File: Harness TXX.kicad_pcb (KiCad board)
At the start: 2 copper layers, 72.1 x 49.5 mm, 88 parts, among them J1 InpConn, J2 InSig, J3 OutConn, J6 SWD, SW1 SW_DPDT, SW2 SW_SPDT, U1 STM32F105RCTx, U2 SN65HVD230, U3 SN65HVD230, U4 TPS562200, U5 AMS1117-3.3, Y1 16MHz

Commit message: Workday progress
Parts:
- removed C18: 10p, Capacitor_SMD:C_0603_1608Metric
- removed C20: 10uF, Capacitor_SMD:C_0603_1608Metric_Pad1.08x0.95mm_HandSolder
- removed C23, C24, C26: 22uF, Capacitor_SMD:C_0603_1608Metric_Pad1.08x0.95mm_HandSolder
- removed C25: 1uF, Capacitor_SMD:C_0603_1608Metric_Pad1.08x0.95mm_HandSolder
- removed JP3, JP4: , Jumper:SolderJumper-2_P1.3mm_Bridged2Bar_Pad1.0x1.5mm
- removed PWR_3V1, PWR_IN1, PWR_IN2: LED, LED_SMD:LED_0603_1608Metric_Pad1.05x0.95mm_HandSolder
- removed PWR_5V1: 100, Resistor_SMD:R_0603_1608Metric_Pad0.98x0.95mm_HandSolder
- removed R14, R16, R20: 120, Resistor_SMD:R_0603_1608Metric
- removed R18: 47, Resistor_SMD:R_0603_1608Metric
- removed R24: 10K, Resistor_SMD:R_0603_1608Metric_Pad0.98x0.95mm_HandSolder
- removed R25: 54.9K, Resistor_SMD:R_0603_1608Metric_Pad0.98x0.95mm_HandSolder
- removed R5, R6, R7: 2k2, Resistor_SMD:R_0603_1608Metric
- removed R8: 100, Resistor_SMD:R_0603_1608Metric
- removed TP2, TP4, TP6, TP8: , TestPoint:TestPoint_THTPad_1.0x1.0mm_Drill0.5mm
- removed U5: AMS1117-3.3, Package_TO_SOT_SMD:SOT-223-3_TabPin2
- added D10: SMLVN6RGB, LED_SMD:LED_ROHM_SMLVN6, F.Cu at (81.5, 80.5)
- added D7: LED, LED_SMD:LED_0603_1608Metric_Pad1.05x0.95mm_HandSolder, F.Cu at (87.4, 71.5)
- added D8: RED, LED_SMD:LED_0603_1608Metric, F.Cu at (97.8, 73.4)
- added D9: DT1446-04TS-7, Global Libraries:SOT95P280X100-6N, F.Cu at (104.4, 80.8)
- added J4: Conn_01x02, Connector_PinHeader_2.54mm:PinHeader_1x02_P2.54mm_Vertical, F.Cu at (111.5, 87.6)
- added SW3: SW_SPDT, Connector_PinHeader_1.27mm:PinHeader_1x03_P1.27mm_Vertical, F.Cu at (98.6, 80.0)
- C1: value 4u7 -> 10uF; footprint Capacitor_SMD:C_0603_1608Metric -> Capacitor_SMD:C_0603_1608Metric_Pad1.08x0.95mm_HandSolder
- C10: value 0u1 -> 100n
- C11, C12, C13, C14: value 100p -> 100n
- C15: value 4.7n -> 1u
- C16: value 4.7n -> 10n
- C17: value 10p -> 0u1
- C19: value 10uF -> 4.7n; footprint Capacitor_SMD:C_0603_1608Metric_Pad1.08x0.95mm_HandSolder -> Capacitor_SMD:C_0603_1608Metric
- C2: value 100n -> 10uF; footprint Capacitor_SMD:C_0603_1608Metric -> Capacitor_SMD:C_0603_1608Metric_Pad1.08x0.95mm_HandSolder
- C21, C22: value 100nF -> 10p; footprint Capacitor_SMD:C_0603_1608Metric_Pad1.08x0.95mm_HandSolder -> Capacitor_SMD:C_0603_1608Metric
- C3, C4: value 100n -> 100nF; footprint Capacitor_SMD:C_0603_1608Metric -> Capacitor_SMD:C_0603_1608Metric_Pad1.08x0.95mm_HandSolder
- C5, C6: value 100n -> 22uF; footprint Capacitor_SMD:C_0603_1608Metric -> Capacitor_SMD:C_0603_1608Metric_Pad1.08x0.95mm_HandSolder
- C7: value 1u -> 1uF; footprint Capacitor_SMD:C_0603_1608Metric -> Capacitor_SMD:C_0603_1608Metric_Pad1.08x0.95mm_HandSolder
- C8: value 10n -> 22uF; footprint Capacitor_SMD:C_0603_1608Metric -> Capacitor_SMD:C_0603_1608Metric_Pad1.08x0.95mm_HandSolder
- C9: value 0u1 -> 4u7
- D1: value 20V -> SD0603S040S0R2; footprint Diode_SMD:D_0603_1608Metric_Pad1.05x0.95mm_HandSolder -> SamacSys_Parts:SD0603
- D2: value 0.7dV -> SD0603S040S0R2; footprint Diode_SMD:D_0603_1608Metric_Pad1.05x0.95mm_HandSolder -> SamacSys_Parts:SD0603
- D3: value RED -> SD0603S040S0R2; footprint LED_SMD:LED_0603_1608Metric -> SamacSys_Parts:SD0603
- D4: value SMLVN6RGB -> SD0603S040S0R2; footprint LED_SMD:LED_ROHM_SMLVN6 -> SamacSys_Parts:SD0603
- D5: value CD143A-SR05 -> 32V; footprint SamacSys_Parts:CD143ASR05 -> Diode_SMD:D_SOD-323
- D6: value CD143A-SR05 -> 0.7dV; footprint SamacSys_Parts:CD143ASR05 -> Diode_SMD:D_SMA
- F1: footprint Fuse:Fuse_0603_1608Metric_Pad1.05x0.95mm_HandSolder -> Fuse:Fuse_1206_3216Metric_Pad1.42x1.75mm_HandSolder
- J1: value InpConn -> DEUTSCH DT Inp; footprint SamacSys_Parts:348300801 -> Global Libraries:DT13-6P
- J2: value InSig -> DEUTSCH DT Data; footprint SamacSys_Parts:348300801 -> Global Libraries:DT13-6P
- J3: value OutConn -> DEUTSCH DT Out; footprint SamacSys_Parts:348300801 -> Global Libraries:DT13-6P
- L1: value 68n -> 4u7; footprint Inductor_SMD:L_0603_1608Metric -> Inductor_SMD:L_Sunlord_MWSA0518_5.4x5.2mm
- L2: value 4u7 -> 68n; footprint Inductor_SMD:L_Sunlord_MWSA0518_5.4x5.2mm -> Inductor_SMD:L_0603_1608Metric
- R1: value Rterm -> 10K; moved to F.Cu
- R12: value 120 -> 220
- R2: value 470 -> 10K
- R21: value 10K -> 47
- R22: value 22 -> 10K
- R23: value 10K -> 22; footprint Resistor_SMD:R_0603_1608Metric_Pad0.98x0.95mm_HandSolder -> Resistor_SMD:R_0603_1608Metric
- R3: value 0 -> 54.9K
- R4: value 2k2 -> 470R; footprint Resistor_SMD:R_0603_1608Metric -> Resistor_SMD:R_0603_1608Metric_Pad0.98x0.95mm_HandSolder
- R9: value 220 -> 100
- SW1: value SW_DPDT -> CAS-120B; footprint SamacSys_Parts:JS202011JCQN -> SamacSys_Parts:CAS120B
- SW2: value SW_SPDT -> CAS-120B; footprint Connector_PinHeader_1.27mm:PinHeader_1x03_P1.27mm_Vertical -> SamacSys_Parts:CAS120B
- U1: value STM32F105RCTx -> LMR51420; footprint Package_QFP:LQFP-64_10x10mm_P0.5mm -> Package_TO_SOT_SMD:SOT-23-6
- U2: value SN65HVD230 -> AMS1117-3.3; footprint Package_SO:SOIC-8_3.9x4.9mm_P1.27mm -> Package_TO_SOT_SMD:SOT-223-3_TabPin2
- U3: value SN65HVD230 -> STM32F105RCTx; footprint Package_SO:SOIC-8_3.9x4.9mm_P1.27mm -> Package_QFP:LQFP-64_10x10mm_P0.5mm
- U4: value TPS562200 -> SN65HVD230; footprint Package_TO_SOT_SMD:SOT-23-6 -> Package_SO:SOIC-8_3.9x4.9mm_P1.27mm
- moved SW1 93.9 mm to (76.7, 94.7), turned to 0 degrees
- moved U2 75.4 mm to (104.9, 74.9), turned to 180 degrees
- moved SW2 75.1 mm to (111.0, 95.5)
- moved C5 73.8 mm to (109.4, 69.3)
- moved D4 68.8 mm to (97.8, 96.5), turned to 180 degrees
- moved D3 66.6 mm to (100.8, 96.5), turned to 180 degrees
- moved J3 65.2 mm to (115.0, 86.6), turned to 180 degrees
- moved U1 63.4 mm to (95.2, 70.0), turned to -90 degrees
- moved JP1 62.2 mm to (104.9, 84.7), turned to 90 degrees
- moved R19 62.1 mm to (107.9, 85.4)
- moved R3 62.0 mm to (98.8, 70.9), turned to 0 degrees
- moved F1 59.1 mm to (74.7, 72.6), turned to -90 degrees
- moved J6 58.3 mm to (98.7, 93.0), turned to 180 degrees
- moved C17 57.4 mm to (102.0, 90.0)
- moved C6 57.4 mm to (109.4, 67.6)
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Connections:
- C1 pad 1: +3.3V -> /VRM/BUCK/V_in
- C11 pad 1: Net-(C11-Pad1) -> +3V3
- C12 pad 1: Net-(C12-Pad1) -> +3V3
- C13 pad 1: Net-(C13-Pad1) -> +3V3
- C14 pad 1: Net-(C14-Pad1) -> +3V3
- C15 pad 1: GND -> +3.3VA
- C15 pad 2: Net-(C15-Pad2) -> GND
- C16 pad 1: GND -> +3.3VA
- C16 pad 2: Net-(C16-Pad2) -> GND
- C17 pad 1: /MCU/HSE_in -> +3V3
- C19 pad 1: /VRM/12V_Out_Protected -> GND
- C19 pad 2: GND -> Net-(C19-Pad2)
- C2 pad 1: +3.3V -> /VRM/BUCK/V_in
- C21 pad 1: /VRM/12V_Out_Protected -> /MCU/HSE_in
- C22 pad 1: /VRM/BUCK/SW -> Net-(C22-Pad1)
- C22 pad 2: /VRM/BUCK/VBST -> GND
- C3 pad 1: +3.3V -> /VRM/BUCK/V_in
- C4 pad 1: +3.3V -> /VRM/BUCK/SW
- C4 pad 2: GND -> /VRM/BUCK/VBST
- C5 pad 1: +3.3V -> +5V
- C6 pad 1: +3.3V -> +5V
- C7 pad 1: +3.3VA -> +5V
- C8 pad 1: +3.3VA -> +3V3
- D1 pad 1: Net-(D1-Pad1) -> +3V3
- D1 pad 2: GND -> /WheelIn2
- D2 pad 1: /VRM/12V_Out_Protected -> /WheelIn2
- D2 pad 2: Net-(D1-Pad1) -> GND
- D3 pad 1: Net-(D3-Pad1) -> +3V3
- D3 pad 2: +3.3V -> /WheelIn1
- D4 pad 1: +3.3V -> /WheelIn1
- D4 pad 2: +3.3V -> GND
- D5 pad 1: GND -> /VRM/DIODE
- D5 pad 2: Net-(C11-Pad1) -> GND
- D6 pad 1: GND -> /VRM/BUCK/V_in
- D6 pad 2: Net-(C12-Pad1) -> /VRM/DIODE
- F1 pad 1: Net-(D1-Pad1) -> /VRM/DIODE
- F1 pad 2: +12V -> +24V
- J1 pad 1: /CAN- -> GND
- J1 pad 2: GND -> /CAN-
- J1 pad 3: +12V -> /PassThru1
- J1 pad 4: /WheelIn1 -> +24V
- J1 pad 6: GND -> /SHIELD
- J1 pad 7: /MISC -> (no net)
- J1 pad 8: /WheelIn2 -> (no net)
- J2 pad 1: +12V -> GND
- J2 pad 2: GND -> /WheelIn2
- J2 pad 3: /WheelIn2 -> /WheelIn1
- J2 pad 4: unconnected-(J2-Pad4) -> +24V
- J2 pad 5: unconnected-(J2-Pad5) -> +5V
- J2 pad 6: unconnected-(J2-Pad6) -> /Extra1
- J2 pad 7: unconnected-(J2-Pad7) -> (no net)
- J2 pad 8: unconnected-(J2-Pad8) -> (no net)
- J3 pad 1: /CAN+ -> GND
- J3 pad 2: GND -> /CAN-
- J3 pad 3: +12V -> /PassThru2
- J3 pad 4: /ENCD1 -> +24V
- J3 pad 5: /CAN- -> /CAN+
- J3 pad 6: GND -> /SHIELD
- J3 pad 7: /MISC -> (no net)
- J3 pad 8: /ENCD2 -> (no net)
- J6 pad 1: +3.3V -> +3V3
- JP1 pad 1: Net-(C13-Pad1) -> Net-(D9-Pad6)
- JP1 pad 2: /MCU/CAN1_H -> /CAN+
- JP2 pad 1: Net-(C11-Pad1) -> Net-(D9-Pad4)
- JP2 pad 2: /MCU/CAN1_L -> /CAN-
- L1 pad 1: +3.3V -> /VRM/BUCK/SW
- L1 pad 2: +3.3VA -> +5V
- L2 pad 1: /VRM/BUCK/SW -> +3V3
- L2 pad 2: /5V -> +3.3VA
- R1 pad 1: /CAN- -> /VRM/BUCK/V_in
- R1 pad 2: /CAN+ -> /VRM/BUCK/EN
- R10 pad 1: Net-(D4-Pad5) -> Net-(D10-Pad6)
- R10 pad 2: /MCU/LED_G -> /MCU/LED_B
- R11 pad 1: Net-(D4-Pad4) -> Net-(D10-Pad5)
- R11 pad 2: /MCU/LED_R -> /MCU/LED_G
- R12 pad 1: Net-(C15-Pad2) -> Net-(D10-Pad4)
- R12 pad 2: Net-(C11-Pad1) -> /MCU/LED_R
- R13 pad 1: Net-(C16-Pad2) -> Net-(C19-Pad2)
- R13 pad 2: Net-(C12-Pad1) -> Net-(D9-Pad4)
- R15 pad 1: Net-(C16-Pad2) -> Net-(C19-Pad2)
- R15 pad 2: Net-(C12-Pad1) -> Net-(D9-Pad4)
- R17 pad 1: Net-(C14-Pad1) -> Net-(D9-Pad6)
- R17 pad 2: Net-(J5-Pad2) -> Net-(J4-Pad2)
- R19 pad 1: Net-(C13-Pad1) -> Net-(D9-Pad6)
- R2 pad 1: /VRM/12V_Out_Protected -> /VRM/BUCK/VFB
- R2 pad 2: Net-(PWR_IN1-Pad2) -> GND
- R21 pad 1: Net-(R21-Pad1) -> /MCU/HSE_out
- R21 pad 2: /MCU/BOOT0 -> Net-(C22-Pad1)
- R22 pad 1: Net-(J6-Pad2) -> Net-(R22-Pad1)
- R22 pad 2: /MCU/SWDIO -> /MCU/BOOT0
- R23 pad 1: /VRM/12V_Out_Protected -> Net-(J6-Pad2)
- R23 pad 2: /VRM/BUCK/EN -> /MCU/SWDIO
- R3 pad 1: /3V3 -> /VRM/BUCK/VFB
- R3 pad 2: Net-(PWR_3V1-Pad2) -> +5V
- R4 pad 1: +3.3V -> GND
- R4 pad 2: /MCU/I2C1_SCL -> Net-(D7-Pad1)
- R9 pad 1: Net-(D4-Pad6) -> Net-(D8-Pad1)
- R9 pad 2: /MCU/LED_B -> GND
- SW1 pad 1: /ENCD1 -> /WheelIn1
- SW1 pad 2: /WheelIn2 -> /PassThru1
- SW1 pad 3: /ENCD2 -> /WheelIn2
- SW2 pad 1: +3.3V -> /WheelIn1
- SW2 pad 2: Net-(R21-Pad1) -> /PassThru2
- SW2 pad 3: GND -> /WheelIn2
- TP5 pad 1: Net-(C13-Pad1) -> Net-(D9-Pad6)
- TP7 pad 1: Net-(C11-Pad1) -> Net-(D9-Pad4)
- U1 pad 1: +3.3V -> GND
- U1 pad 2: /MCU/PC13 -> /VRM/BUCK/SW
- U1 pad 3: /MCU/PC14 -> /VRM/BUCK/V_in
- U1 pad 4: /MCU/PC15 -> /VRM/BUCK/VFB
- U1 pad 5: /MCU/HSE_in -> /VRM/BUCK/EN
- U1 pad 6: /MCU/HSE_out -> /VRM/BUCK/VBST
- U2 pad 1: /MCU/CAN1_TX -> GND
- U2 pad 2: GND -> +3V3
- U2 pad 3: +3V3 -> +5V
- U3 pad 1: /MCU/CAN2_TX -> +3V3
- U3 pad 2: GND -> /MCU/PC13
- U3 pad 3: +3V3 -> /MCU/PC14
- U3 pad 4: /MCU/CAN2_RX -> /MCU/PC15
- U3 pad 5: +3V3 -> /MCU/HSE_in
- U3 pad 6: Net-(C12-Pad1) -> /MCU/HSE_out
- U3 pad 7: Net-(C14-Pad1) -> unconnected-(U3-Pad7)
- U3 pad 8: GND -> /MCU/PC0
- U4 pad 1: GND -> /MCU/CAN1_TX
- U4 pad 2: /VRM/BUCK/SW -> GND
- U4 pad 3: /VRM/12V_Out_Protected -> +3V3
- U4 pad 4: /VRM/BUCK/VFB -> /MCU/CAN1_RX
- U4 pad 5: /VRM/BUCK/EN -> unconnected-(U4-Pad5)
- U4 pad 6: /VRM/BUCK/VBST -> Net-(D9-Pad4)
- Y1 pad 3: Net-(C18-Pad1) -> Net-(C22-Pad1)
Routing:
- net /CAN-: track 119.6 -> 0.00 mm
- net /CAN+: track 103.1 -> 0.00 mm
- net /MISC: track 87.6 -> 0.00 mm
- net /WheelIn2: track 68.0 -> 0.00 mm
- net /WheelIn1: track 59.0 -> 0.00 mm
- net +12V: track 42.5 -> 0.00 mm, vias 3 -> 0
- net /ENCD2: track 16.5 -> 0.00 mm
- net /ENCD1: track 13.4 -> 0.00 mm
- net /VRM/BUCK/SW: track 10.5 -> 0.00 mm
- net /VRM/BUCK/EN: track 6.87 -> 0.00 mm
- net /VRM/BUCK/VFB: track 6.64 -> 0.00 mm
- net /3V3: track 6.30 -> 0.00 mm
- net Net-(PWR_5V1-Pad2): track 2.48 -> 0.00 mm
- net Net-(PWR_IN1-Pad2): track 2.43 -> 0.00 mm
- net /VRM/BUCK/VBST: track 2.21 -> 0.00 mm
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- removed copper zone on F.Cu, net +12V
- removed copper zone on F.Cu, net /3V3
- removed copper zone on F.Cu, net /5V
- removed copper zone on F.Cu, net /VRM/12V_Out_Protected
- removed copper zone on F.Cu, net GND
- removed copper zone on F.Cu, net Net-(D1-Pad1)
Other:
- board size 72.1 x 49.5 mm -> 91.2 x 58.9 mm

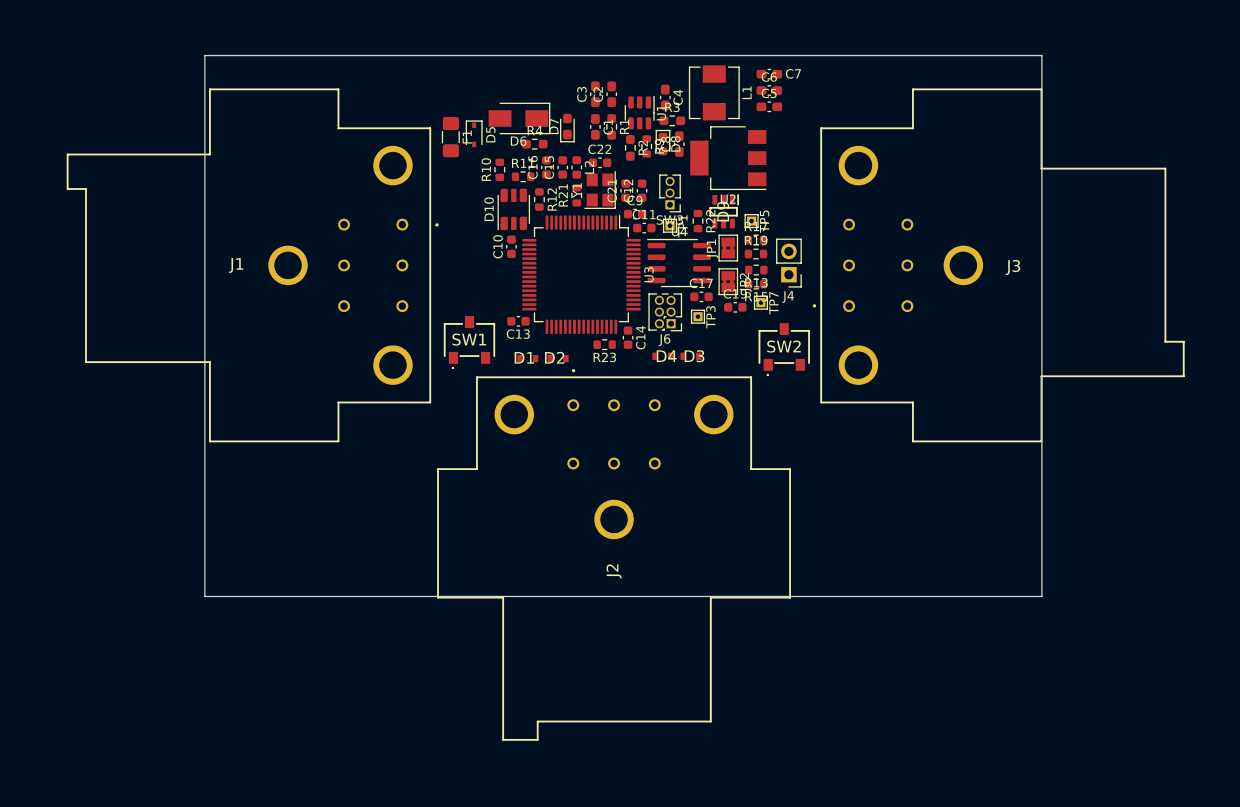
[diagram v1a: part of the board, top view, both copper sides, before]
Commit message: resized board
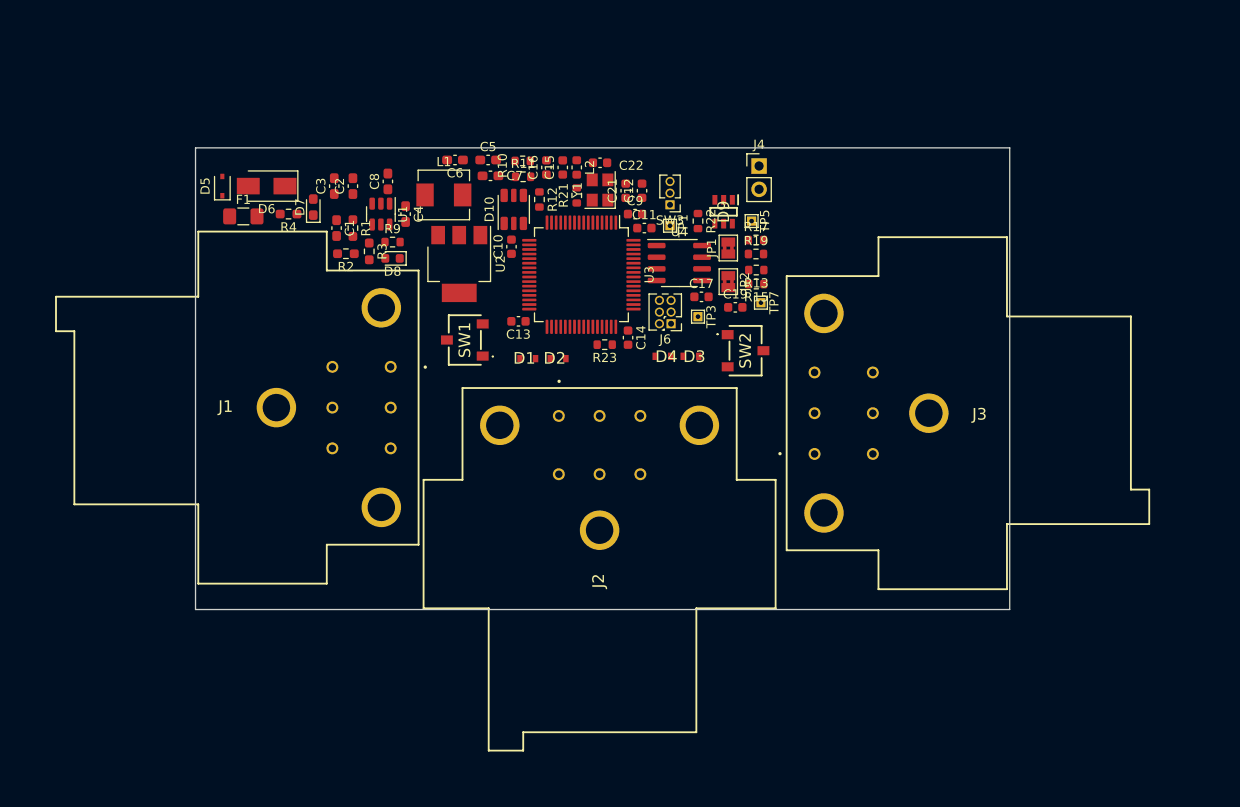
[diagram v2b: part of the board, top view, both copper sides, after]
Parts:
- moved R3 36.0 mm to (65.8, 85.1), turned to -90 degrees
- moved C6 35.1 mm to (75.1, 75.1), turned to 180 degrees
- moved R2 33.1 mm to (63.2, 85.3), turned to 180 degrees
- moved C7 32.3 mm to (79.0, 76.9)
- moved C8 32.0 mm to (67.8, 77.5)
- moved D8 32.0 mm to (68.3, 85.9), turned to 180 degrees
- moved U2 31.5 mm to (75.6, 86.5), turned to -90 degrees
- moved L1 31.5 mm to (73.9, 78.9), turned to 0 degrees
- moved C5 31.2 mm to (78.7, 75.1)
- moved C4 31.0 mm to (69.7, 81.0)
- moved C1 30.3 mm to (62.2, 82.5)
- moved R1 30.3 mm to (64.0, 82.5)
- moved U1 30.3 mm to (67.1, 81.0)
- moved C3 30.2 mm to (62.0, 78.0)
- moved C2 29.9 mm to (64.0, 78.0)
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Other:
- board size 91.2 x 58.9 mm -> 88.7 x 50.3 mm

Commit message: changes
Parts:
- moved C8 17.0 mm to (80.2, 89.2)
- moved J4 7.32 mm to (112.0, 82.1), turned to 180 degrees
- moved L2 4.75 mm to (85.5, 79.7), turned to 0 degrees
- moved R12 3.64 mm to (85.1, 75.9)
- moved C16 3.30 mm to (88.4, 75.9)
- moved J3 2.79 mm to (111.3, 99.9)
- moved TP5 2.35 mm to (108.0, 79.5)
- moved D4 2.27 mm to (96.3, 98.2)
- moved D5 2.26 mm to (48.5, 79.8)
- moved R17 1.97 mm to (108.1, 81.9)
- moved D3 1.80 mm to (100.1, 98.1)
- moved R19 1.71 mm to (108.0, 83.7)
- moved R13 1.58 mm to (108.0, 85.5)
- moved C1 1.48 mm to (62.1, 81.1)
- moved R1 1.47 mm to (64.1, 81.1)
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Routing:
- net GND: track 0.00 -> 18.4 mm, vias 0 -> 25
- net /VRM/BUCK/EN: track 0.00 -> 5.83 mm, vias 0 -> 2
- net /VRM/BUCK/VFB: track 0.00 -> 4.67 mm
- net +3V3: track 0.00 -> 2.14 mm
- net Net-(D7-Pad1): track 0.00 -> 1.92 mm
- net Net-(D8-Pad1): track 0.00 -> 1.79 mm
- net /VRM/BUCK/VBST: track 0.00 -> 1.70 mm
- net /VRM/BUCK/SW: track 0.00 -> 1.25 mm
- added copper zone on F.Cu, net +24V
- added copper zone on F.Cu, net /VRM/BUCK/SW
- added copper zone on F.Cu, net /VRM/BUCK/V_in
- added copper zone on F.Cu, net /VRM/DIODE
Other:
- board size 88.7 x 50.3 mm -> 88.7 x 50.8 mm

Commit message: Workday 12/4/22
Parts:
- moved L2 0.80 mm to (85.9, 79.0)
- moved C8 0.36 mm to (80.5, 89.2)
- moved C6 0.20 mm to (75.1, 74.9)
- moved C7 0.10 mm to (79.0, 76.9)
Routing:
- net +3V3: track 2.14 -> 83.2 mm, vias 0 -> 4
- net +5V: track 0.31 -> 45.2 mm, vias 0 -> 4
- net GND: track 18.4 -> 44.5 mm, vias 25 -> 31
- net /WheelIn2: track 0.00 -> 7.74 mm
- net /MCU/LED_B: track 0.00 -> 7.69 mm, vias 0 -> 2
- net Net-(J6-Pad2): track 0.00 -> 7.39 mm, vias 0 -> 1
- net Net-(D10-Pad4): track 0.00 -> 7.31 mm
- net Net-(C19-Pad2): track 0.00 -> 7.03 mm
- net +3.3VA: track 0.00 -> 6.92 mm
- net /MCU/CAN1_RX: track 0.00 -> 6.83 mm, vias 0 -> 2
- net /MCU/LED_G: track 0.00 -> 5.94 mm
- net Net-(J4-Pad2): track 0.00 -> 5.85 mm
- net /PassThru2: track 0.00 -> 5.80 mm
- net /MCU/LED_R: track 0.00 -> 5.65 mm
- net /MCU/HSE_in: track 0.00 -> 5.58 mm
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- added copper zone on F.Cu, net +3V3
- added copper zone on F.Cu, net +5V
- added copper zone on F.Cu, net Net-(D9-Pad4)
- added copper zone on F.Cu, net Net-(D9-Pad6)

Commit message: Had been modifying a file on my computer and not git on accident. Adding updated PCB to Git
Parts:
- removed the SW2 at (106.8, 95.9)
- added G***: LOGO, custom symbols:flaggers, B.Cu at (88.6, 90.9)
- added TP1: TestPoint, TestPoint:TestPoint_Plated_Hole_D3.0mm, F.Cu at (61.0, 73.4)
- added TP2: TestPoint, TestPoint:TestPoint_Plated_Hole_D3.0mm, F.Cu at (116.3, 101.6)
- added TP3: TestPoint, TestPoint:TestPoint_Plated_Hole_D3.0mm, F.Cu at (117.9, 73.4)
- added TP4: TestPoint, TestPoint:TestPoint_Plated_Hole_D3.0mm, F.Cu at (62.0, 100.6)
- J1, J2, J3: footprint Global Libraries:DT13-6P -> Connector_Molex:Molex_Micro-Fit_3.0_43045-0600_2x03_P3.00mm_Horizontal
- SW1: value CAS-120B -> SW_SPDT; footprint SamacSys_Parts:CAS120B -> SamacSys_Parts:CAS120A1
- moved D6 29.3 mm to (71.1, 101.3)
- moved D7 28.1 mm to (71.9, 104.1), turned to 0 degrees
- moved D5 27.8 mm to (66.0, 101.3), turned to -90 degrees
- moved R4 26.8 mm to (68.1, 104.1)
- moved R10 24.2 mm to (84.1, 99.4)
- moved U1 24.0 mm to (78.5, 101.1)
- moved R2 23.8 mm to (77.0, 104.1)
- moved C12 23.7 mm to (86.6, 100.3), turned to -90 degrees
- moved R1 23.4 mm to (75.7, 101.3)
- moved C3 23.3 mm to (72.9, 97.4)
- moved R3 23.0 mm to (81.5, 100.8), turned to 90 degrees
- moved F1 23.0 mm to (68.8, 96.5), turned to 90 degrees
- moved J2 22.6 mm to (88.5, 77.8), turned to 0 degrees
- moved D4 22.2 mm to (99.6, 76.2), turned to 90 degrees
- moved C2 21.8 mm to (71.1, 97.5)
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- renumbered SW3 to SW2, TP7 to TP11, TP1 to TP5, TP3 to TP7, TP5 to TP9
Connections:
- J1 pad 3: /PassThru1 -> /PassThru
- J3 pad 3: /PassThru2 -> /PassThru
- SW1 pad 2: /PassThru1 -> /PassThru
- U3 pad 14: /MCU/LED_R -> /MCU/PB0
- U3 pad 15: /MCU/LED_G -> /MCU/PB1
- U3 pad 16: /MCU/LED_B -> /MCU/PB2
- U3 pad 26: /MCU/PB0 -> /MCU/LED_R
- U3 pad 27: /MCU/PB1 -> /MCU/LED_G
- U3 pad 28: /MCU/PB2 -> /MCU/LED_B
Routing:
- net /CAN+: track 0.00 -> 90.7 mm
- net /CAN-: track 0.00 -> 90.3 mm
- net /PassThru: track 0.00 -> 76.4 mm, vias 0 -> 2
- net /SHIELD: track 0.00 -> 76.3 mm, vias 0 -> 2
- net +24V: track 0.00 -> 63.2 mm, vias 0 -> 5
- net /WheelIn1: track 0.00 -> 46.4 mm, vias 0 -> 6
- net /WheelIn2: track 7.74 -> 42.3 mm, vias 0 -> 4
- net Net-(D9-Pad6): track 0.00 -> 25.9 mm
- net +5V: track 45.2 -> 67.7 mm, vias 4 -> 5
- net /Extra1: track 0.00 -> 21.5 mm, vias 0 -> 1
- net GND: track 44.5 -> 60.4 mm, vias 31 -> 28
- net Net-(D9-Pad4): track 5.50 -> 17.7 mm
- net /MCU/SWDIO: track 0.00 -> 8.21 mm
- net +3V3: track 83.2 -> 91.1 mm
- net /MCU/CAN1_RX: track 6.83 -> 14.6 mm
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- added copper zone on F.Cu, net GND
- added copper zone on F.Cu, net Net-(C19-Pad2)
- added copper zone on F.Cu, net Net-(C22-Pad1)
- added copper zone on F.Cu, net Net-(J4-Pad2)
- removed copper zone on F.Cu, net +24V
- removed copper zone on F.Cu, net /VRM/BUCK/SW
- removed copper zone on F.Cu, net Net-(D9-Pad4)
- removed copper zone on F.Cu, net Net-(D9-Pad6)
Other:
- board size 88.7 x 50.8 mm -> 63.5 x 35.3 mm
